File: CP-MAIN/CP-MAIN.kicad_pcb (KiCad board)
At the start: 2 copper layers, 60 x 90 mm, 32 parts, among them J1 power, J2 Serial, J3 USB_A, J4 w-Sensor1, J5 i2c, J6 w-Sensor2, J7 w-Sensor3, Q1 Q_NMOS_GDS, Q2 Q_NMOS_GDS, Q3 Q_NMOS_GDS, U1 R-783.3-0.5, U2 AE-ATMEGA328-MINI, U3 TWELITE_DIP

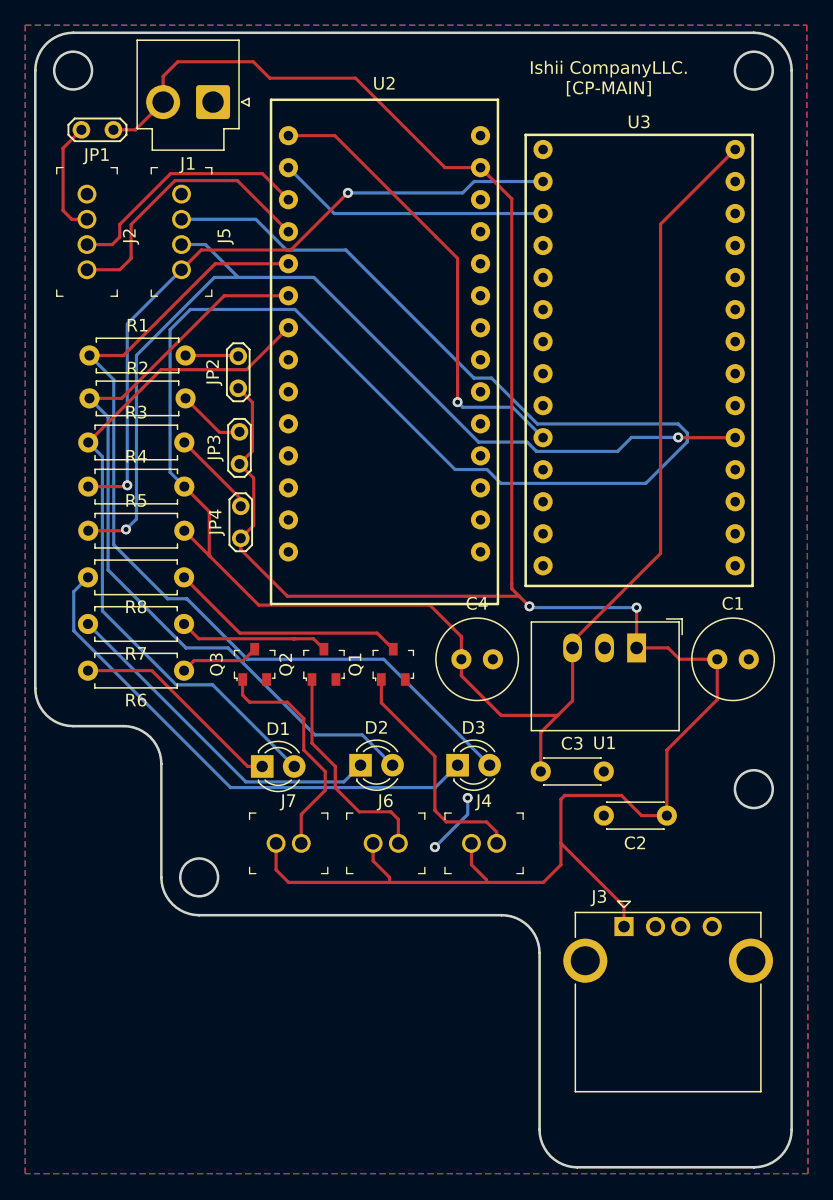
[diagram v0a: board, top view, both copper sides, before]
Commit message: ・CP-MAIN水位センサアナログ入力用に変更
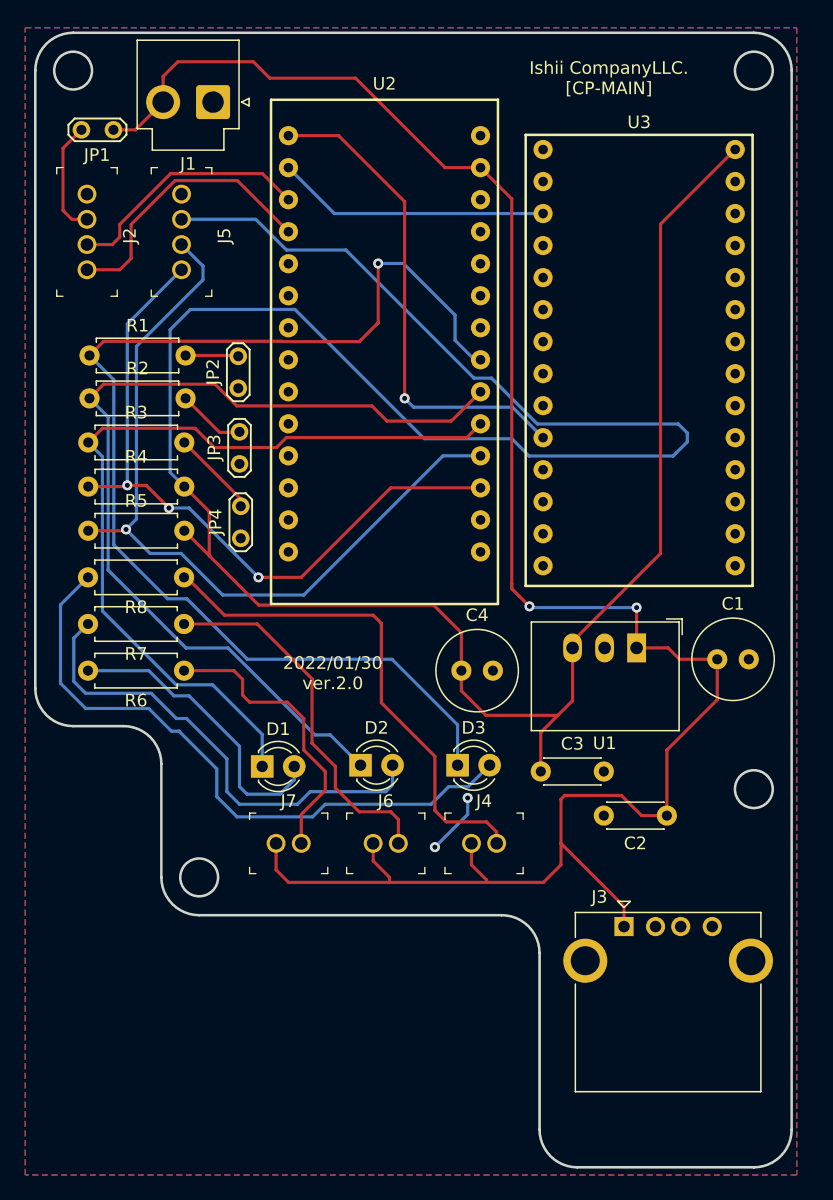
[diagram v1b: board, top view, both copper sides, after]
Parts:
- removed Q1, Q2, Q3: Q_NMOS_GDS, digikey-footprints:SOT-23W
- moved C4 0.90 mm to (144.6, 101.2)
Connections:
- D1 pad 1: Net-(D1-Pad1) -> SP3
- D1 pad 2: SP3 -> Net-(D1-Pad2)
- D2 pad 1: Net-(D2-Pad1) -> SP2
- D2 pad 2: SP2 -> Net-(D2-Pad2)
- D3 pad 1: Net-(D3-Pad1) -> SP1
- D3 pad 2: SP1 -> Net-(D3-Pad2)
- J3 pad 5: (no net) -> GND
- J5 pad 3: TW-SDA -> SDA
- J5 pad 4: TW-SCL -> SCL
- JP2 pad 1: 5V -> GND
- JP3 pad 1: 5V -> GND
- JP4 pad 1: 5V -> GND
- R4 pad 1: TW-SCL -> SCL
- R5 pad 1: TW-SDA -> SDA
- R6 pad 1: Net-(Q3-Pad2) -> w-Sensor3
- R6 pad 2: Net-(D1-Pad1) -> Net-(D1-Pad2)
- R7 pad 1: Net-(Q2-Pad2) -> w-Sensor2
- R7 pad 2: Net-(D2-Pad1) -> Net-(D2-Pad2)
- R8 pad 1: Net-(Q1-Pad2) -> w-Sensor1
- R8 pad 2: Net-(D3-Pad1) -> Net-(D3-Pad2)
- U2 pad 17: Net-(U2-Pad17) -> SCL
- U2 pad 18: Net-(U2-Pad18) -> SDA
- U2 pad 19: Net-(U2-Pad19) -> SP3
- U2 pad 20: Net-(U2-Pad20) -> SP2
- U2 pad 21: Net-(U2-Pad21) -> SP1
- U2 pad 5: SP1 -> Net-(U2-Pad5)
- U2 pad 6: SP2 -> Net-(U2-Pad6)
- U2 pad 7: SP3 -> Net-(U2-Pad7)
- U3 pad 19: TW-SDA -> Net-(U3-Pad19)
- U3 pad 2: TW-SCL -> Net-(U3-Pad2)
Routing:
- net TW-SDA: track 79.0 -> 0.00 mm, vias 2 -> 0
- net SDA: track 0.00 -> 63.7 mm, vias 0 -> 1
- net SCL: track 0.00 -> 56.0 mm, vias 0 -> 3
- net TW-SCL: track 53.6 -> 0.00 mm, vias 2 -> 0
- net Net-(D3-Pad2): track 0.00 -> 50.7 mm
- net Net-(D3-Pad1): track 41.0 -> 0.00 mm
- net 5V: track 199.0 -> 160.8 mm
- net Net-(D2-Pad2): track 0.00 -> 38.1 mm
- net Net-(D2-Pad1): track 27.4 -> 0.00 mm
- net Net-(D1-Pad2): track 0.00 -> 23.8 mm
- net SP1: track 71.7 -> 93.4 mm, vias 0 -> 1
- net w-Sensor1: track 18.9 -> 40.5 mm
- net Net-(Q1-Pad2): track 19.0 -> 0.00 mm
- net Net-(D1-Pad1): track 17.0 -> 0.00 mm
- net w-Sensor2: track 17.5 -> 29.9 mm
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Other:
- board text added: "2022/01/30 ver.2.0"
